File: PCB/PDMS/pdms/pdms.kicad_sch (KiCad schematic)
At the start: 53 parts, among them IC19 STM32L496ZGT6, IC20 AT25SF128A-SHB-T, J1 DBG, J2 6473427-1, J3 N01_036_6501_001, Y1 16Mhz, Y2 32KHz

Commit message: Final touch PDMS
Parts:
- added J4: DBG, Connector_Molex:Molex_PicoBlade_53047-0610_1x06_P1.25mm_Vertical, symbol Connector_Generic:Conn_02x03_Counter_Clockwise
- added J5: SAFETY, Connector_Molex:Molex_PicoBlade_53047-0410_1x04_P1.25mm_Vertical, symbol Connector:Conn_01x04_Male
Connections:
- net +12V: now also J5.3 (Pin_3)
- net +3.3V: now also J4.1 (Pin_1)
- net +5V: now also J4.3 (Pin_3), J5.4 (Pin_4)
- net GND: now also J2.10, J2.12, J2.14, J2.56, J2.57, J4.2 (Pin_2), J5.2 (Pin_2)
- net NRST: now also J4.4 (Pin_4)
- net SAFETY_IN: now also J5.1 (Pin_1)
- net SWCLK: now also J4.5 (Pin_5)
- net SWDIO: now also J4.6 (Pin_6)
- no-connect marks 42 -> 41

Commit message: Sitched via side
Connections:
- net HP_MOS7: now also J2.3; no longer J2.2
- net LP_MOS7: now also J2.2; no longer J2.3
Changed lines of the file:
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@@
     )
   )
-  (global_label "HP_MOS7" (shape input) (at 332.105 159.385 180) (fields_autoplaced)
+  (global_label "HP_MOS7" (shape input) (at 332.105 161.925 180) (fields_autoplaced)
     (effects (font (size 1.27 1.27)) (justify right))
-    (property "Intersheet References" "${INTERSHEET_REFS}" (id 0) (at 320.9229 159.3056 0)
+    (property "Intersheet References" "${INTERSHEET_REFS}" (id 0) (at 320.9229 161.8456 0)
       (effects (font (size 1.27 1.27)) (justify right) hide)
     )
@@
     )
   )
-  (global_label "LP_MOS7" (shape input) (at 332.105 161.925 180) (fields_autoplaced)
+  (global_label "LP_MOS7" (shape input) (at 332.105 159.385 180) (fields_autoplaced)
     (effects (font (size 1.27 1.27)) (justify right))
-    (property "Intersheet References" "${INTERSHEET_REFS}" (id 0) (at 321.2252 161.8456 0)
+    (property "Intersheet References" "${INTERSHEET_REFS}" (id 0) (at 321.2252 159.3056 0)
       (effects (font (size 1.27 1.27)) (justify right) hide)
     )
@@
       (reference "#PWR0378") (unit 1) (value "+5V") (footprint "")
     )
+    (path "/5e0d1f91-4fae-411e-a2b8-95f4b4fcadc5/a440236e-372c-41e7-add7-4b8781296e41"
+      (reference "#PWR0379") (unit 1) (value "GND") (footprint "")
+    )
     (path "/c4ca1078-fd8d-4af6-b44e-00e6aed0cd5e"
       (reference "#PWR0380") (unit 1) (value "GND") (footprint "")
@@
     )
     (path "/5e0d1f91-4fae-411e-a2b8-95f4b4fcadc5/50334e3e-f97b-45b1-a00b-5148d7178b01"
-      (reference "#PWR?") (unit 1) (value "+5V") (footprint "")
-    )
-    (path "/5e0d1f91-4fae-411e-a2b8-95f4b4fcadc5/a440236e-372c-41e7-add7-4b8781296e41"
-      (reference "#PWR?") (unit 1) (value "GND") (footprint "")
+      (reference "#PWR0383") (unit 1) (value "+5V") (footprint "")
     )
     (path "/12a3a5c1-ac79-4586-9274-31138d63f5db/afc75a69-04d1-4636-8ea3-b3fe3061a65f"
@@
       (reference "R168") (unit 1) (value "1.2k") (footprint "Resistor_SMD:R_0402_1005Metric")
     )
-    (path "/5e0d1f91-4fae-411e-a2b8-95f4b4fcadc5/064f68cd-33aa-440f-a561-ea7f56e641ba"
-      (reference "R?") (unit 1) (value "1k") (footprint "Resistor_SMD:R_0402_1005Metric")
-    )
     (path "/5e0d1f91-4fae-411e-a2b8-95f4b4fcadc5/e56fe53b-8d81-47aa-bdfc-2ba550736a36"
-      (reference "R?") (unit 1) (value "1k") (footprint "Resistor_SMD:R_0402_1005Metric")
+      (reference "R169") (unit 1) (value "1k") (footprint "Resistor_SMD:R_0402_1005Metric")
+    )
+    (path "/5e0d1f91-4fae-411e-a2b8-95f4b4fcadc5/064f68cd-33aa-440f-a561-ea7f56e641ba"
+      (reference "R170") (unit 1) (value "1k") (footprint "Resistor_SMD:R_0402_1005Metric")
     )
     (path "/b84c6964-5564-4d57-8b96-ee4462f76a3a"

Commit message: Changed main power connector, added USB-C, added BLE - not wired yet
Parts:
- removed J3: N01_036_6501_001, PDMS_Additional:N010366501001, symbol pdms_additional:N01_036_6501_001
- added D37: BAT54SW, Package_TO_SOT_SMD:SOT-323_SC-70, symbol Diode:BAT54SW
- added J3: 7461383, PDMS_Additional:7461383, symbol pdms_additional:7461383
- added R171: 1.2k, Resistor_SMD:R_0402_1005Metric, symbol Device:R_Small
- added R172: 2.2k, Resistor_SMD:R_0402_1005Metric, symbol Device:R_Small
- added U11: SPBTLE-RF, RF_Module:ST_SPBTLE, symbol RF_Bluetooth:SPBTLE-RF
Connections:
- net +12V: now also J3.1, J3.10, J3.11, J3.12, J3.13, J3.14, J3.15, J3.16, J3.2, J3.3, J3.4, J3.5, J3.6, J3.7, J3.8, J3.9, R171.2
- net +3.3V: now also D37.2
- net +5V: now also J1.5 (Pin_5); no longer J1.3 (Pin_3)
- net GND: now also J1.3 (Pin_3), D37.1, R172.1, U11.6 (GND); no longer J1.2 (Pin_2)
- net NRST: now also J1.2 (Pin_2); no longer J1.4 (Pin_4)
- net SWCLK: now also J1.6 (Pin_6), J4.6 (Pin_6); no longer J1.5 (Pin_5), J4.5 (Pin_5)
- net SWDIO: now also J1.4 (Pin_4), J4.5 (Pin_5); no longer J1.6 (Pin_6), J4.6 (Pin_6)
- net at IC19.47 (PB1): now also D37.3, R171.1, R172.2
- net USB_OTG_FS_DM_OPT renamed USB-C/USB_D-
- net USB_OTG_FS_DP_OPT renamed USB-C/USB_D+
- no-connect marks 41 -> 43
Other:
- added sheet USB-C (usb-c.kicad_sch)
- note added: "CHANGE THIS - VALUES"

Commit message: USB-C symbol changed
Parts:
- U11: footprint RF_Module:ST_SPBTLE -> PDMS_Additional:XCVR_SPBTLE-RF
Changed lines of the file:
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@@
       (effects (font (size 1.27 1.27)) (justify left))
     )
-    (property "Footprint" "RF_Module:ST_SPBTLE" (id 2) (at 54.61 275.844 0)
+    (property "Footprint" "PDMS_Additional:XCVR_SPBTLE-RF" (id 2) (at 54.61 275.844 0)
       (effects (font (size 1.27 1.27)) hide)
     )
@@
     )
     (path "/3bd3a751-7d87-46c8-83fc-77ed2a9e4c3b"
-      (reference "U11") (unit 1) (value "SPBTLE-RF") (footprint "RF_Module:ST_SPBTLE")
+      (reference "U11") (unit 1) (value "SPBTLE-RF") (footprint "PDMS_Additional:XCVR_SPBTLE-RF")
     )
     (path "/ad53e72b-8846-45b3-8238-61a743b440ac/7f51cc6c-2d89-42ac-9175-ff66b0ad958b"

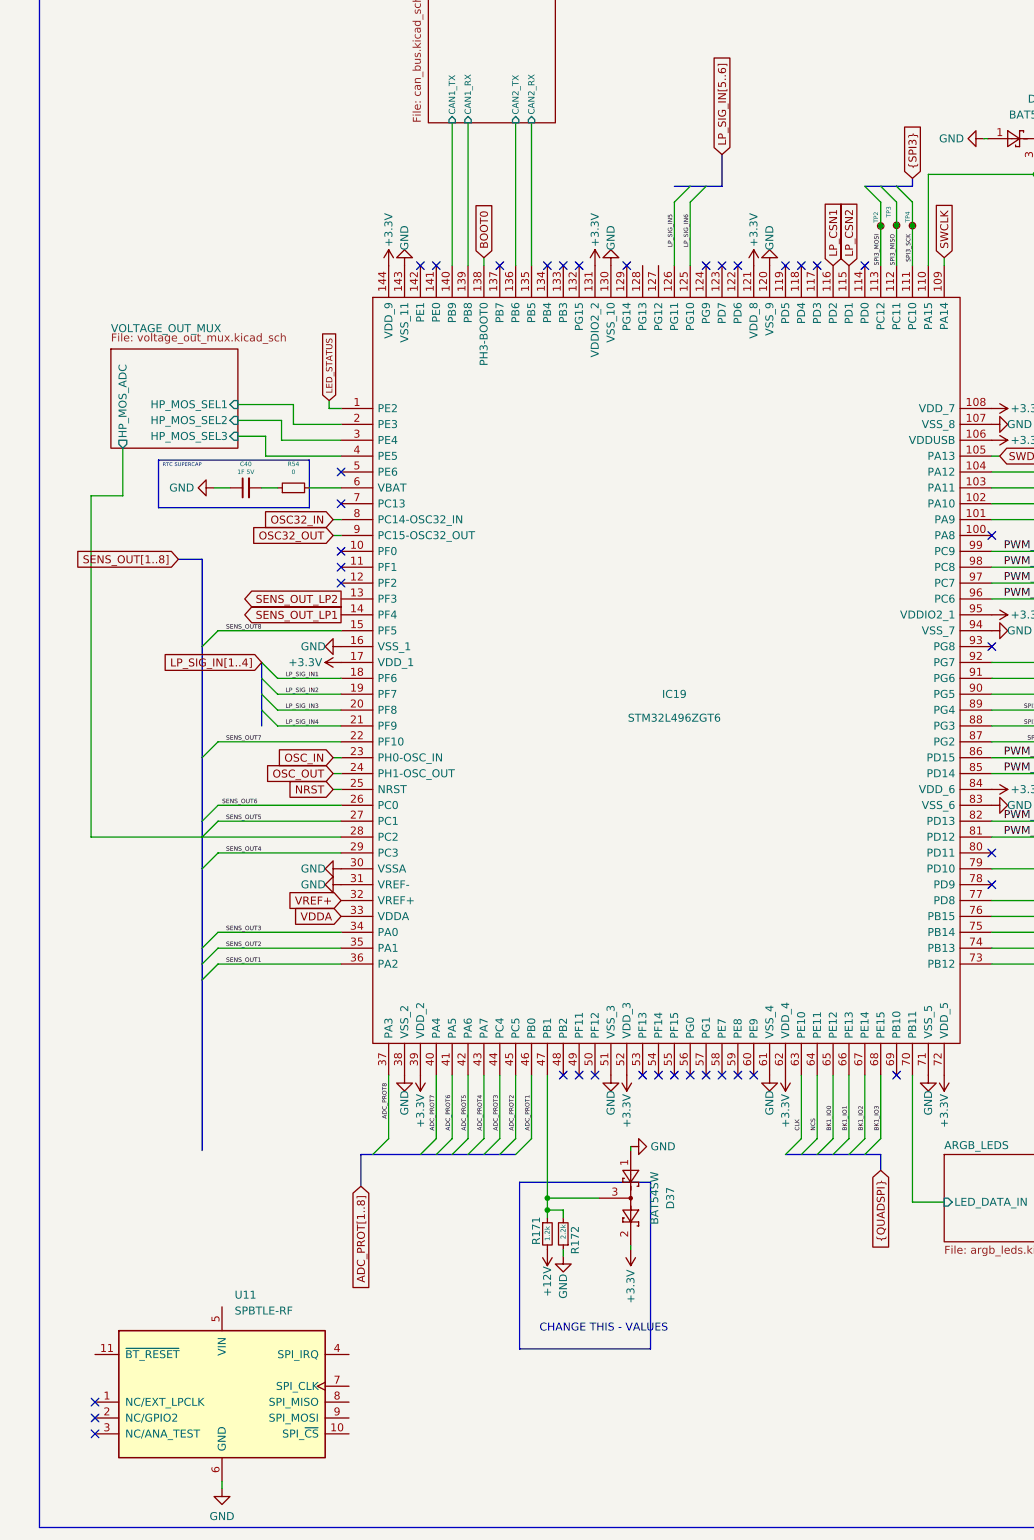
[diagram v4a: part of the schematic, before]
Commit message: Added BLE module
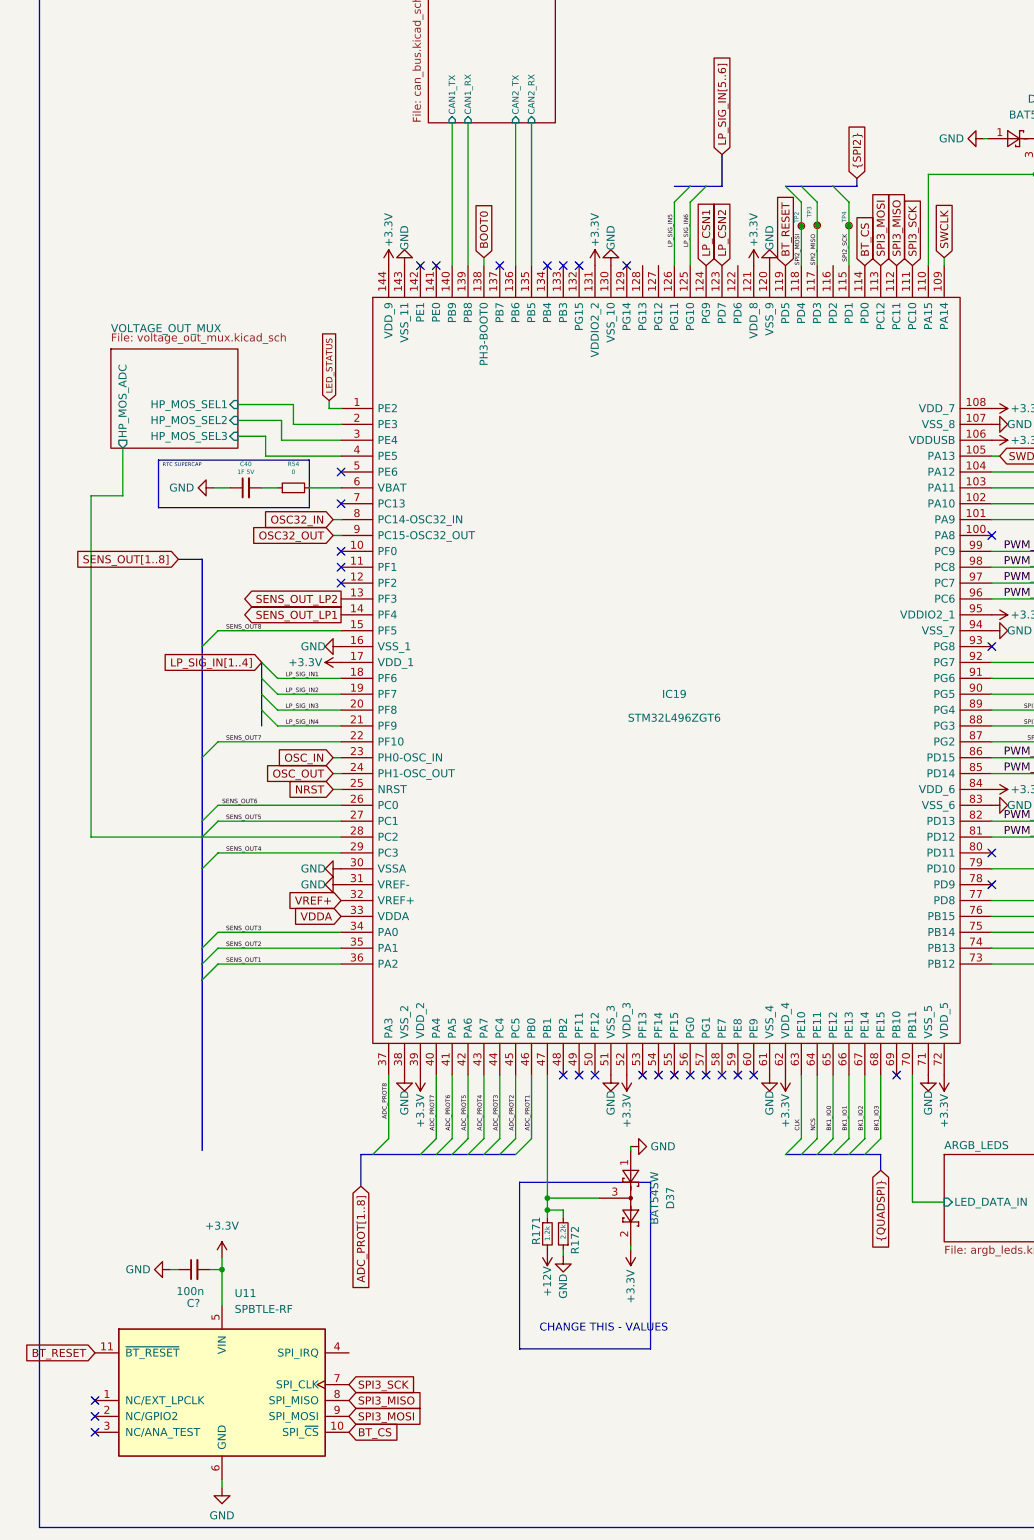
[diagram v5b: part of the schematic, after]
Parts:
- added C?: 100n, Capacitor_SMD:C_0402_1005Metric, symbol Device:C_Small
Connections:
- net +3.3V: now also U11.5 (VIN), C?.2
- net GND: now also C?.1
- net LP_CSN1: now also IC19.124 (PG9); no longer IC19.116 (PD2)
- net LP_CSN2: now also IC19.123 (PD7); no longer IC19.115 (PD1)
- net SPI3_MISO: now also U11.8 (SPI_MISO); no longer TP3.1
- net SPI3_MOSI: now also U11.9 (SPI_MOSI); no longer TP2.1
- net SPI3_SCK: now also U11.7 (SPI_CLK); no longer TP4.1
- net BT_CS: now reaches IC19.114 (PD0)
- net BT_CS: now also U11.10 (SPI_~{CS})
- net SPI2_MISO: now reaches IC19.117 (PD3)
- net SPI2_MISO: now also TP3.1
- net SPI2_MOSI: now reaches IC19.118 (PD4)
- net SPI2_MOSI: now also TP2.1
- net BT_RESET: now reaches IC19.119 (PD5)
- net BT_RESET: now also U11.11 (~{BT_RESET})
- new net SPI2_SCK: IC19.115 (PD1), TP4.1
- no-connect marks 43 -> 36
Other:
- moved on the sheet: TP2, TP3, TP4

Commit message: Minor chnages
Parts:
- gave numbers to parts that had none: 1
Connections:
- net BT_IRQ: now reaches IC19.122 (PD6)
- net BT_IRQ: now also U11.4 (SPI_IRQ)
- no-connect marks 36 -> 38
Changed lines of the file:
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@@
   (no_connect (at 21.59 269.24))
   (no_connect (at 21.59 266.7))
+  (no_connect (at 111.76 82.55))
+  (no_connect (at 109.22 82.55))
   (no_connect (at 124.46 212.09))
   (no_connect (at 127 212.09))
@@
     )
   )
+  (global_label "BT_IRQ" (shape input) (at 62.23 256.54 0) (fields_autoplaced)
+    (effects (font (size 1.27 1.27)) (justify left))
+    (property "Intersheet References" "${INTERSHEET_REFS}" (id 0) (at 71.0536 256.4606 0)
+      (effects (font (size 1.27 1.27)) (justify left) hide)
+    )
+  )
   (global_label "SWCLK" (shape input) (at 395.605 62.23 0) (fields_autoplaced)
     (effects (font (size 1.016 1.016)) (justify left))
@@
     )
   )
+  (global_label "BT_IRQ" (shape input) (at 124.46 82.55 90) (fields_autoplaced)
+    (effects (font (size 1.27 1.27)) (justify left))
+    (property "Intersheet References" "${INTERSHEET_REFS}" (id 0) (at 124.3806 73.7264 90)
+      (effects (font (size 1.27 1.27)) (justify left) hide)
+    )
+  )
   (global_label "HP_MOS3" (shape input) (at 358.775 182.245 0) (fields_autoplaced)
     (effects (font (size 1.27 1.27)) (justify left))
@@
   (symbol (lib_id "Device:C_Small") (at 37.465 243.205 90) (unit 1)
     (in_bom yes) (on_board yes)
-    (property "Reference" "C?" (id 0) (at 38.4175 248.6025 90)
+    (property "Reference" "C87" (id 0) (at 38.4175 248.6025 90)
       (effects (font (size 1.27 1.27)) (justify left))
     )
@@
   (symbol (lib_id "power:GND") (at 33.655 243.205 270) (unit 1)
     (in_bom yes) (on_board yes) (fields_autoplaced)
-    (property "Reference" "#PWR?" (id 0) (at 27.305 243.205 0)
+    (property "Reference" "#PWR0199" (id 0) (at 27.305 243.205 0)
       (effects (font (size 1.27 1.27)) hide)
     )
@@
   (symbol (lib_id "power:+3.3V") (at 41.91 241.3 0) (unit 1)
     (in_bom yes) (on_board yes) (fields_autoplaced)
-    (property "Reference" "#PWR?" (id 0) (at 41.91 245.11 0)
+    (property "Reference" "#PWR0195" (id 0) (at 41.91 245.11 0)
       (effects (font (size 1.27 1.27)) hide)
     )
@@
       (reference "#PWR0194") (unit 1) (value "GND") (footprint "")
     )
+    (path "/ddb55a5d-1d9f-438e-ad33-388f02ae308e"
+      (reference "#PWR0195") (unit 1) (value "+3.3V") (footprint "")
+    )
     (path "/12a3a5c1-ac79-4586-9274-31138d63f5db/1fb17df7-5dae-46f3-a6b6-e041d2a7295d"
       (reference "#PWR0196") (unit 1) (value "GND") (footprint "")
@@
       (reference "#PWR0198") (unit 1) (value "+5V") (footprint "")
     )
+    (path "/aac675ba-4dfb-4f5f-b99a-00e193fb7236"
+      (reference "#PWR0199") (unit 1) (value "GND") (footprint "")
+    )
     (path "/820f510a-62ce-49d5-912e-fe3ad7cb4b3b"
       (reference "#PWR0201") (unit 1) (value "+3.3V") (footprint "")
@@
       (reference "#PWR0398") (unit 1) (value "GND") (footprint "")
     )
-    (path "/aac675ba-4dfb-4f5f-b99a-00e193fb7236"
-      (reference "#PWR?") (unit 1) (value "GND") (footprint "")
-    )
-    (path "/ddb55a5d-1d9f-438e-ad33-388f02ae308e"
-      (reference "#PWR?") (unit 1) (value "+3.3V") (footprint "")
-    )
     (path "/12a3a5c1-ac79-4586-9274-31138d63f5db/afc75a69-04d1-4636-8ea3-b3fe3061a65f"
       (reference "BZ1") (unit 1) (value "Buzzer") (footprint "Buzzer_Beeper:Buzzer_12x9.5RM7.6")
@@
       (reference "C86") (unit 1) (value "0.1uF") (footprint "Capacitor_SMD:C_0402_1005Metric")
     )
+    (path "/2be129da-81ff-4519-bcb4-5feec934ba3e"
+      (reference "C87") (unit 1) (value "100n") (footprint "Capacitor_SMD:C_0402_1005Metric")
+    )
     (path "/6d28209d-3875-451f-b3ee-e74429ea47eb"
       (reference "C88") (unit 1) (value "C") (footprint "Capacitor_THT:CP_Radial_D12.5mm_P5.00mm")
@@
       (reference "C91") (unit 1) (value "100n") (footprint "Resistor_SMD:R_0402_1005Metric")
     )
-    (path "/2be129da-81ff-4519-bcb4-5feec934ba3e"
-      (reference "C?") (unit 1) (value "100n") (footprint "Capacitor_SMD:C_0402_1005Metric")
-    )
     (path "/1bbf27ea-c2a2-447a-8999-6ade1a66fd07/34207786-e978-4c45-a5a6-f374522bab76/489a5137-a2b9-4263-917a-4451b07c9591"

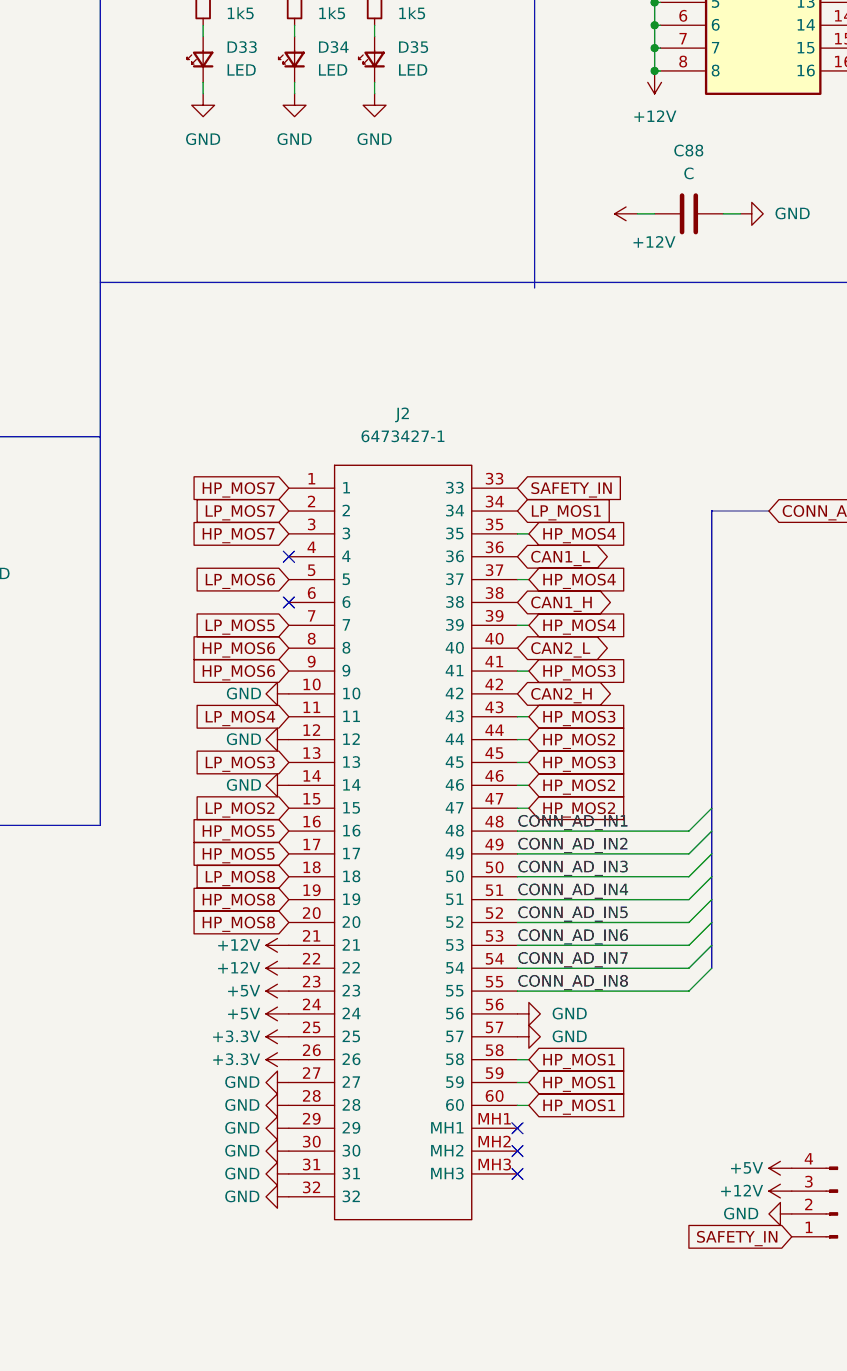
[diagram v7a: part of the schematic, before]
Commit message: Added fuse output for sensors
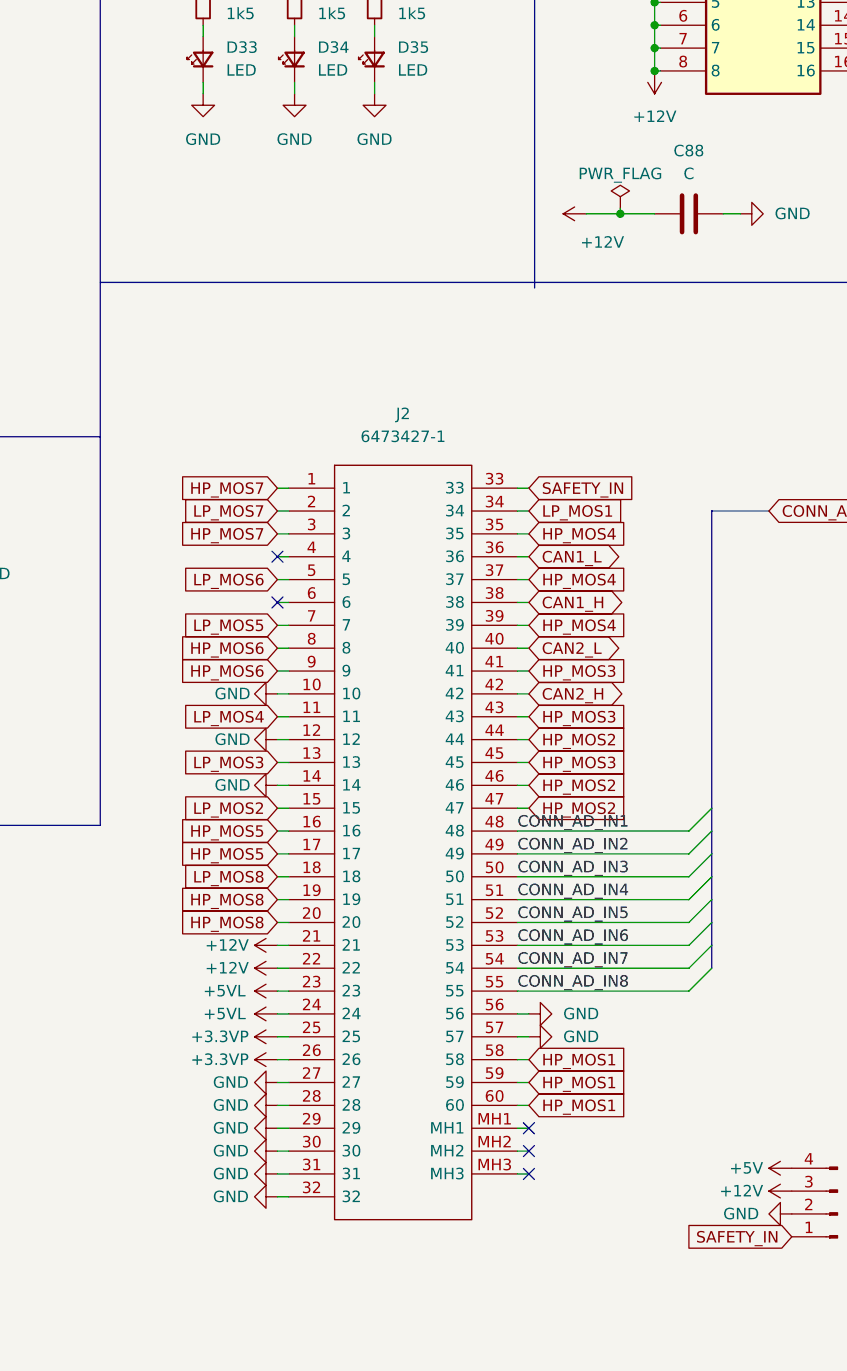
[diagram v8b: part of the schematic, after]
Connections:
- net +3.3V: no longer J2.25, J2.26
- net +5V: no longer J2.23, J2.24
- new net +3.3VP: J2.25, J2.26
- new net +5VL: J2.23, J2.24
